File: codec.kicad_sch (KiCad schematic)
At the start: 8 parts, among them U8 WM8988LGECN/V

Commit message: More stuff
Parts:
- removed C23: 4.7u, Capacitor_SMD:C_0603_1608Metric, symbol Device:C
- removed C25, C26: 4.7u, Capacitor_SMD:CP_Elec_5x4.5, symbol Device:C_Polarized
- added C22, C23: 4.7u, Capacitor_SMD:CP_Elec_5x4.5, symbol Device:C_Polarized
- added C25, C26: 4.7u, Capacitor_SMD:C_0603_1608Metric, symbol Device:C
- added C27: 1u, Capacitor_SMD:C_0603_1608Metric, symbol Device:C
- C19: renamed from C20; LCSC C48579280 -> (none)
- C20: renamed from C21; LCSC C48579280 -> (none)
- C24: value 4.7u -> 1u; LCSC C48579280 -> (none)
- renumbered C22 to C21, U8 to U7
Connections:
- net +3V3A: now also C25.2, C26.2
- net GND: now also C22.2, C23.2; no longer C21.2, C24.1, U7.13 (HPGND), U7.18 (AGND)
- net IN_Left: now also C24.1; no longer U7.24 (LINPUT1)
- net IN_Right: now also C27.1; no longer U7.23 (RINPUT1)
- net at C24.2: now also U7.24 (LINPUT1); no longer U7.19 (VREF)
- net at U7.20 (VMID): now also C22.1
- new net: C27.2, U7.23 (RINPUT1)
- new net: C23.1, U7.19 (VREF)
- new net GNDA: C21.2, C25.1, C26.1, U7.13 (HPGND), U7.18 (AGND)

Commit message: Fixes
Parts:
- added C18, C21: 220u, Capacitor_SMD:CP_Elec_5x5.4, symbol Device:C_Polarized
- renumbered C19 to C17, C20 to C19, C21 to C20
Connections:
- net OUT_Left: now also C21.2; no longer U7.12 (LOUT1)
- net OUT_Right: now also C18.2; no longer U7.11 (ROUT1)
- new net: C18.1, U7.11 (ROUT1)
- new net: C21.1, U7.12 (LOUT1)

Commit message: started compact layout
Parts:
- removed C20, C22, C23: 4.7u, Capacitor_SMD:CP_Elec_5x4.5, symbol Device:C_Polarized
- added C20, C22, C23: 4.7u, Capacitor_SMD:C_0603_1608Metric, symbol Device:C
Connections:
- net +3V3 is gone; now on net +3V3D: U7.25 (MODE)
- net GND: now also C22.1, C23.1
- net GNDA: now also C20.2
- net at U7.20 (VMID): now also C22.2
- net at U7.19 (VREF): now also C23.2
- net at U7.9 (HPCOM): now also C20.1

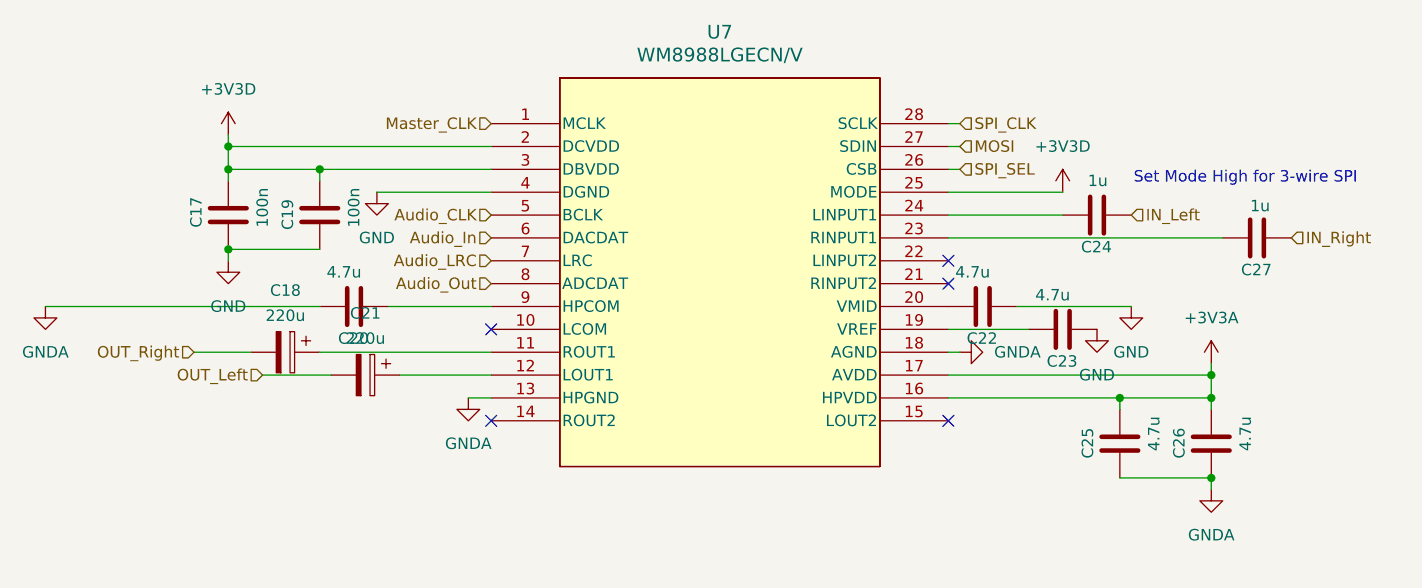
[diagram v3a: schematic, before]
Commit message: feat: start hat version
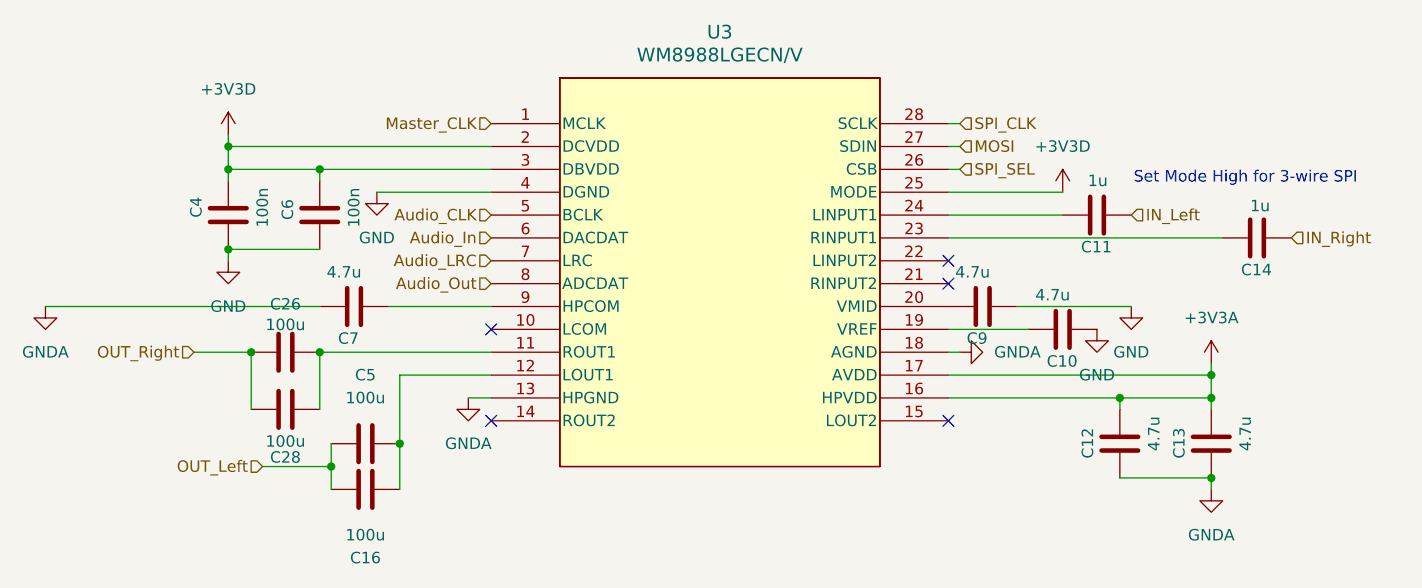
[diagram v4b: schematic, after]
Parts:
- removed C18, C21: 220u, Capacitor_SMD:CP_Elec_5x5.4, symbol Device:C_Polarized
- added C16, C26, C28, C5: 100u, Capacitor_SMD:C_1206_3216Metric, symbol Device:C
- renumbered C23 to C10, C24 to C11, C25 to C12, C26 to C13, C27 to C14, C17 to C4, C19 to C6, C20 to C7, C22 to C9, U7 to U3
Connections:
- net OUT_Left: now also C16.1, C5.1
- net OUT_Right: now also C26.1, C28.1
- net at U3.11 (ROUT1): now also C26.2, C28.2
- net at U3.12 (LOUT1): now also C16.2, C5.2

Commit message: More capacitor layed
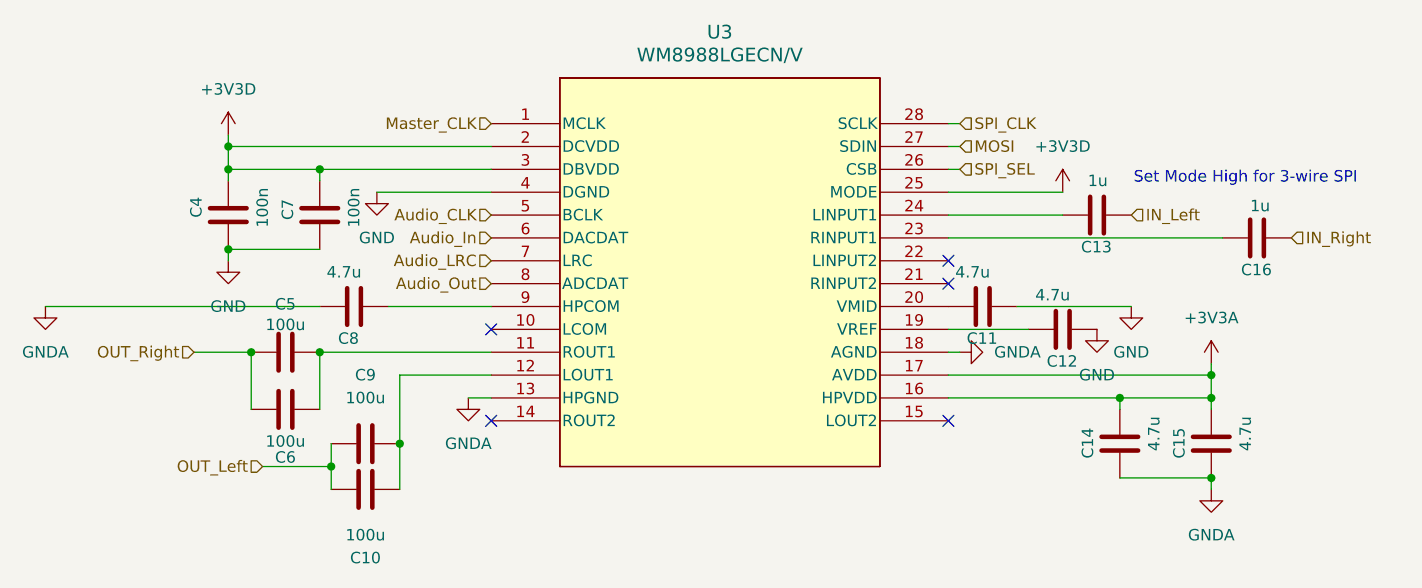
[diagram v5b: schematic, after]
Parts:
- renumbered C16 to C10, C9 to C11, C10 to C12, C11 to C13, C12 to C14, C13 to C15, C14 to C16, C26 to C5, C28 to C6, C6 to C7, C7 to C8, C5 to C9

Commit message: feat: pretty much done
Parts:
- U3: footprint footprints:QFN28_4X4_CIR-M -> footprints:QFN28_4X4_CIR
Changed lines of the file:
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@@
 		(on_board yes)
 		(dnp no)
-		(fields_autoplaced yes)
 		(property "Reference" "U3"
 			(at 130.81 64.77 0)
@@
 			)
 		)
-		(property "Footprint" "footprints:QFN28_4X4_CIR-M"
+		(property "Footprint" "footprints:QFN28_4X4_CIR"
 			(at 105.41 74.93 0)
 			(effects

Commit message: feat: overhaul
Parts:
- C12: renamed from C4; footprint Capacitor_SMD:C_0603_1608Metric -> Capacitor_SMD:C_0402_1005Metric; LCSC (none) -> C307331
- C15: renamed from C7; footprint Capacitor_SMD:C_0603_1608Metric -> Capacitor_SMD:C_0402_1005Metric; LCSC (none) -> C307331
- C16: renamed from C8; footprint Capacitor_SMD:C_0603_1608Metric -> Capacitor_SMD:C_0402_1005Metric; LCSC (none) -> C23733
- C19: renamed from C11; footprint Capacitor_SMD:C_0603_1608Metric -> Capacitor_SMD:C_0402_1005Metric; LCSC (none) -> C23733
- C20: renamed from C12; footprint Capacitor_SMD:C_0603_1608Metric -> Capacitor_SMD:C_0402_1005Metric; LCSC (none) -> C23733
- C21: renamed from C13; footprint Capacitor_SMD:C_0603_1608Metric -> Capacitor_SMD:C_0402_1005Metric; LCSC (none) -> C52923
- C22: renamed from C14; footprint Capacitor_SMD:C_0603_1608Metric -> Capacitor_SMD:C_0402_1005Metric; LCSC (none) -> C23733
- C23: renamed from C15; footprint Capacitor_SMD:C_0603_1608Metric -> Capacitor_SMD:C_0402_1005Metric; LCSC (none) -> C23733
- C24: renamed from C16; footprint Capacitor_SMD:C_0603_1608Metric -> Capacitor_SMD:C_0402_1005Metric; LCSC (none) -> C52923
- renumbered C5 to C13, C6 to C14, C9 to C17, C10 to C18, U3 to U5
